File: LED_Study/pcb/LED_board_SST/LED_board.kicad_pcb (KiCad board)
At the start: 2 copper layers, 25.4 x 25.4 mm, 4 parts

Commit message: new boards
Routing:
- net /Vin: track 13.8 -> 0.00 mm
- net /GND: track 13.8 -> 0.00 mm
- net Net-(D3-Pad1): track 12.3 -> 0.00 mm
- net Net-(D1-Pad1): track 11.9 -> 0.00 mm
- added copper zone on F.Cu, net /GND
- added copper zone on F.Cu, net /Vin
- added copper zone on F.Cu, net Net-(D1-Pad1)
- added copper zone on F.Cu, net Net-(D3-Pad1)
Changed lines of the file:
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@@
     (pad_to_mask_clearance 0)
     (pcbplotparams
-      (layerselection 0x00010fc_ffffffff)
+      (layerselection 0x00010a8_7fffffff)
       (plot_on_all_layers_selection 0x0000000_00000000)
       (disableapertmacros false)
@@
   (gr_circle (center 100 100) (end 112.7 100)
     (stroke (width 0.1) (type default)) (fill none) (layer "Edge.Cuts"))
-  (segment (start 92 95.198) (end 95.198 92) (width 0.75) (layer "F.Cu") (net 1))
-  (segment (start 92 98.9) (end 92 95.198) (width 0.75) (layer "F.Cu") (net 1))
-  (segment (start 95.198 92) (end 98.9 92) (width 0.75) (layer "F.Cu") (net 1))
-  (segment (start 92 108) (end 98.9 108) (width 0.75) (layer "F.Cu") (net 3))
-  (segment (start 92 108) (end 92 101.1) (width 0.75) (layer "F.Cu") (net 3))
   (via (at 92 108) (size 3) (drill 1.5) (layers "F.Cu" "B.Cu") (free) (net 3))
-  (segment (start 108 92) (end 108 98.9) (width 0.75) (layer "F.Cu") (net 4))
-  (segment (start 108 92) (end 101.1 92) (width 0.75) (layer "F.Cu") (net 4))
   (via (at 108 92) (size 3) (drill 1.5) (layers "F.Cu" "B.Cu") (free) (net 4))
-  (segment (start 101.1 108) (end 105.36 108) (width 0.75) (layer "F.Cu") (net 6))
-  (segment (start 105.36 108) (end 108 105.36) (width 0.75) (layer "F.Cu") (net 6))
-  (segment (start 108 105.36) (end 108 101.1) (width 0.75) (layer "F.Cu") (net 6))
+  (zone (net 4) (net_name "/GND") (layer "F.Cu") (hatch edge 0.5)
+    (connect_pads (clearance 0.5))
+    (min_thickness 0.25) (filled_areas_thickness no)
+    (fill yes (thermal_gap 0.5) (thermal_bridge_width 0.5))
+    (polygon
+      (pts
+        (xy 100 100)
+        (xy 100 87)
+        (xy 113 87)
+        (xy 113 100)
+      )
+    )
+  )
+  (zone (net 1) (net_name "Net-(D1-Pad1)") (layer "F.Cu") (hatch edge 0.5)
+    (priority 2)
+    (connect_pads (clearance 0.5))
+    (min_thickness 0.25) (filled_areas_thickness no)
+    (fill yes (thermal_gap 0.5) (thermal_bridge_width 0.5))
+    (polygon
+      (pts
+        (xy 100 100)
+        (xy 87 100)
+        (xy 87 87)
+        (xy 100 87)
+      )
+    )
+  )
+  (zone (net 3) (net_name "/Vin") (layer "F.Cu") (hatch edge 0.5)
+    (priority 3)
+    (connect_pads (clearance 0.5))
+    (min_thickness 0.25) (filled_areas_thickness no)
+    (fill yes (thermal_gap 0.5) (thermal_bridge_width 0.5))
+    (polygon
+      (pts
+        (xy 100 100)
+        (xy 87 100)
+        (xy 87 113)
+        (xy 100 113)
+      )
+    )
+  )
+  (zone (net 6) (net_name "Net-(D3-Pad1)") (layer "F.Cu") (hatch edge 0.5)
+    (priority 1)
+    (connect_pads (clearance 0.5))
+    (min_thickness 0.25) (filled_areas_thickness no)
+    (fill yes (thermal_gap 0.5) (thermal_bridge_width 0.5))
+    (polygon
+      (pts
+        (xy 100 100)
+        (xy 113 100)
+        (xy 113 113)
+        (xy 100 113)
+      )
+    )
+  )
 )

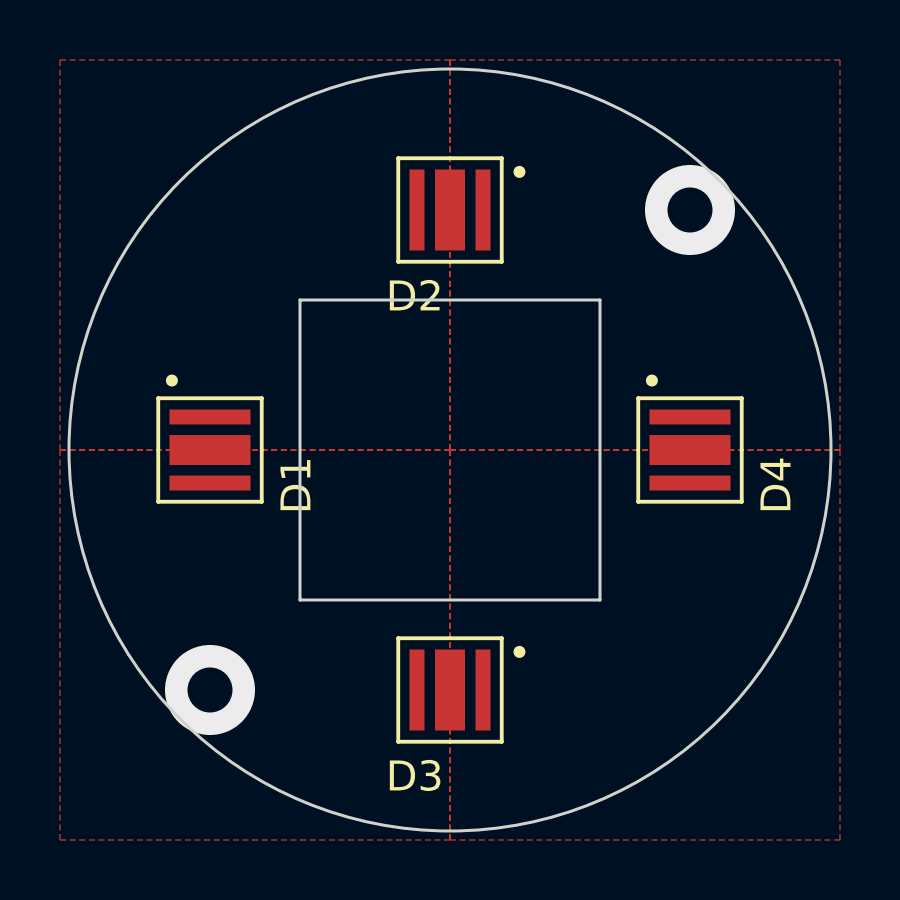
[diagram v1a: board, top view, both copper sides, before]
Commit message: updated boards and ordered from PCBway
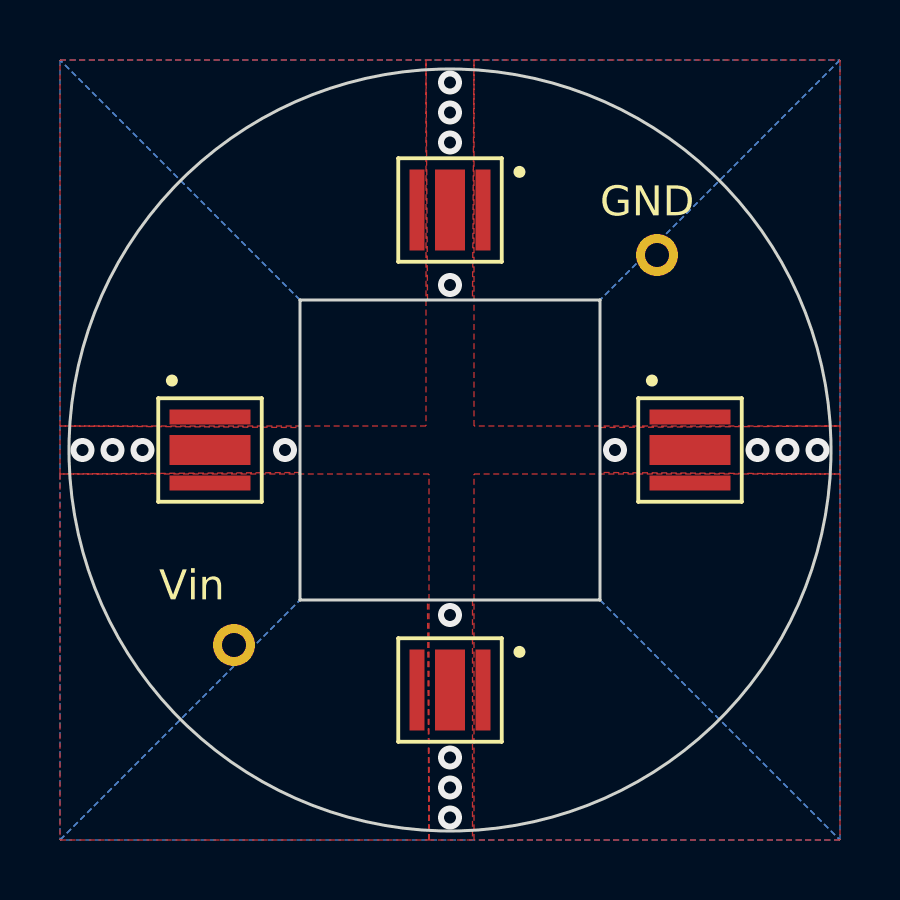
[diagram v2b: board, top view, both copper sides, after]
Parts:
- added J1: Conn_01x01_Pin, Connector_PinHeader_1.00mm:PinHeader_1x01_P1.00mm_Vertical, F.Cu at (92.8, 106.5)
- added J2: Conn_01x01_Pin, Connector_PinHeader_1.00mm:PinHeader_1x01_P1.00mm_Vertical, F.Cu at (106.9, 93.5)
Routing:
- net unconnected-(D4-EXP-Pad3): vias 0 -> 4
- net unconnected-(D3-EXP-Pad3): vias 0 -> 4
- net unconnected-(D2-EXP-Pad3): vias 0 -> 4
- net unconnected-(D1-EXP-Pad3): vias 0 -> 4
- net /Vin: vias 1 -> 0
- net /GND: vias 1 -> 0
- added copper zone on B.Cu, net unconnected-(D1-EXP-Pad3)
- added copper zone on F.Cu, net unconnected-(D1-EXP-Pad3)
- added copper zone on B.Cu, net unconnected-(D2-EXP-Pad3)
- added copper zone on F.Cu, net unconnected-(D2-EXP-Pad3)
- added copper zone on B.Cu, net unconnected-(D3-EXP-Pad3)
- added copper zone on F.Cu, net unconnected-(D3-EXP-Pad3)
- added copper zone on B.Cu, net unconnected-(D4-EXP-Pad3)
- added copper zone on F.Cu, net unconnected-(D4-EXP-Pad3)
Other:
- board text added: "GND"
- board text added: "Vin"
